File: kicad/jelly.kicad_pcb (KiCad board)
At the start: 2 copper layers, 59.9 x 32.9 mm, 29 parts, among them M1 PAGER_MOTOR, M2 PAGER_MOTOR, P1 CONN_01X01, P10 CONN_01X01, P11 CONN_01X01, P12 CONN_01X01, P13 CONN_01X01, P14 CONN_01X01, P15 CONN_01X01, P2 CONN_01X01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

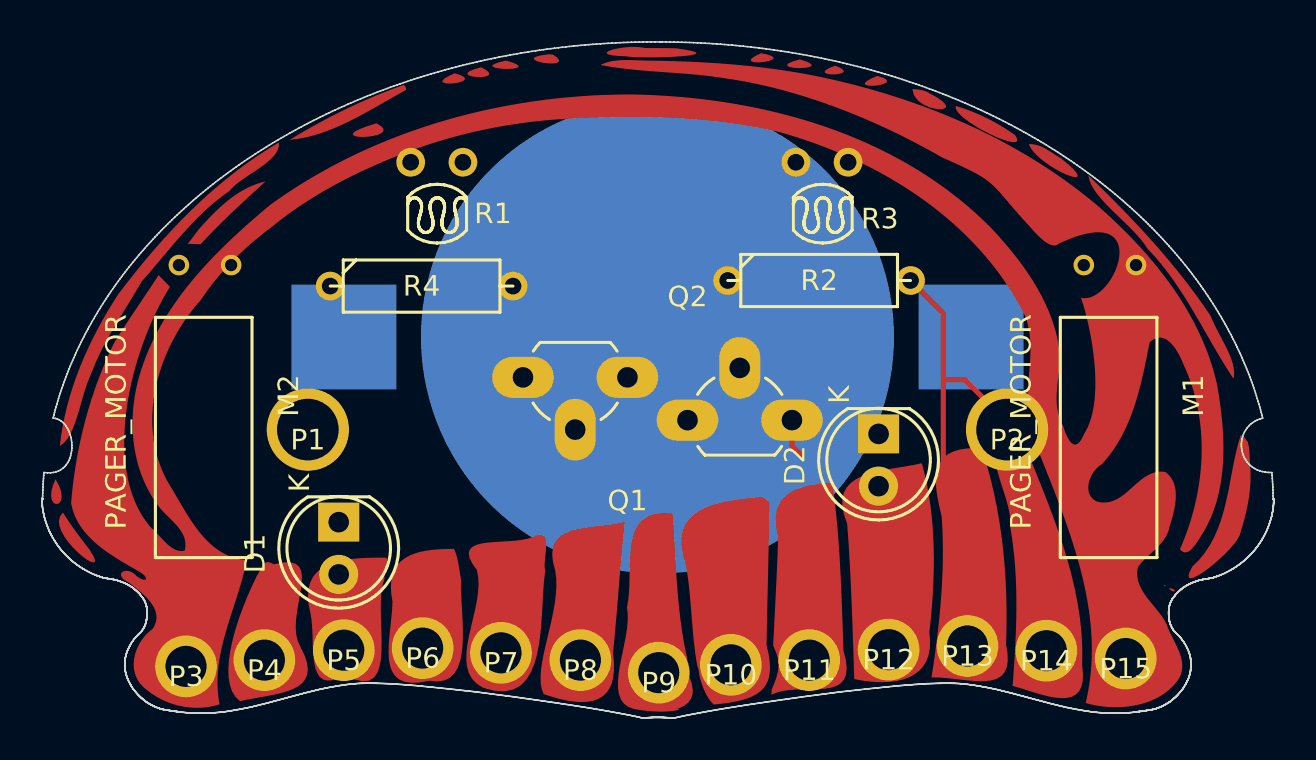
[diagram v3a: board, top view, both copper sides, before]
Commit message: Try and fit things in around CR2450
doesn't look possible
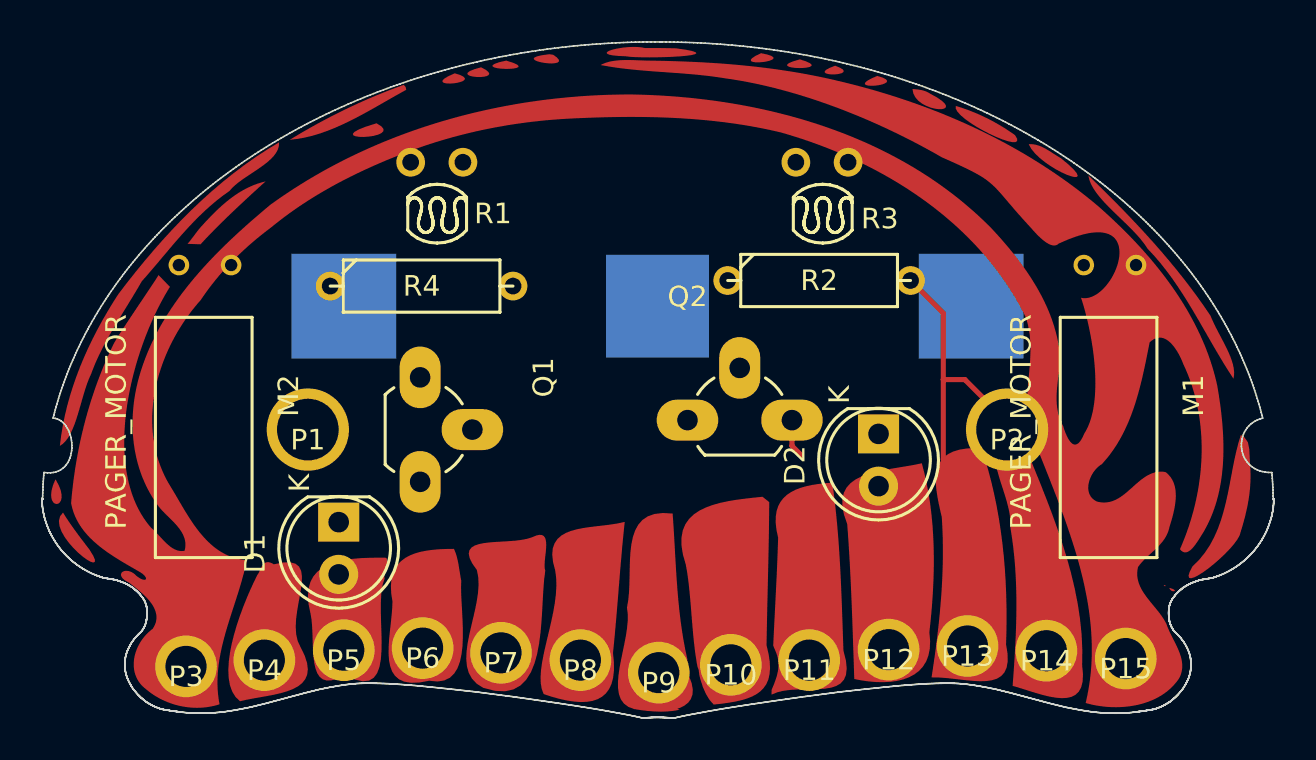
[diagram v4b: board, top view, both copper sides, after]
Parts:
- BT1: footprint custom:cr2450_holder -> cr2450_holder
- moved Q1 10.1 mm to (138.5, 80.5), turned to 270 degrees
- moved BT1 1.50 mm to (150.0, 77.0)
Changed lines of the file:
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@@
   (general
     (links 30)
-    (no_connects 26)
+    (no_connects 28)
     (area 119.662141 58.550827 180.412426 101.693013)
     (thickness 1.6)
@@
     (pad_to_mask_clearance 0)
     (aux_axis_origin 0 0)
-    (visible_elements FFFFFF7F)
+    (visible_elements FFFCFF7F)
     (pcbplotparams
       (layerselection 0x010f0_ffffffff)
@@
     (add_net Vout2)
   )
-  (module custom:cr2450_holder (layer B.Cu)
-    (at 150 78.5 180)
+  (module cr2450_holder (layer B.Cu)
+    (at 150 77 180)
     (fp_text reference BT1 (at 0 -0.5 180) (layer B.SilkS)
       (effects (font (size 1 1) (thickness 0.15)) (justify mirror))
@@
       (effects (font (size 1 1) (thickness 0.15)) (justify mirror))
     )
-    (fp_arc (start -9 8) (end -12 8) (angle -180) (layer B.SilkS) (width 0.15))
-    (fp_arc (start 9 8) (end 6 8) (angle -180) (layer B.SilkS) (width 0.15))
+    (fp_circle (center 0 0) (end 12.25 0.5) (layer B.SilkS) (width 0.15))
+    (fp_arc (start 9 5) (end 6 8) (angle -90) (layer B.SilkS) (width 0.15))
+    (fp_arc (start -9 6) (end -12 8) (angle -112.6198649) (layer B.SilkS) (width 0.15))
+    (fp_arc (start 0 12) (end 6 8) (angle -112.6198649) (layer B.SilkS) (width 0.15))
     (fp_line (start -12 8) (end -12 -7) (layer B.SilkS) (width 0.15))
     (fp_line (start -12 -7) (end -4 -14) (layer B.SilkS) (width 0.15))
@@
     (fp_line (start 4 -14) (end 12 -7) (layer B.SilkS) (width 0.15))
     (fp_line (start 12 -7) (end 12 8) (layer B.SilkS) (width 0.15))
-    (pad 1 smd rect (at -15.25 0 180) (size 5.1 5.1) (layers B.Cu B.Paste B.Mask)
+    (pad 2 smd rect (at -15.25 0 180) (size 5.1 5.1) (layers B.Cu B.Paste B.Mask)
+      (net 6 GND))
+    (pad 2 smd rect (at 15.25 0 180) (size 5.1 5.1) (layers B.Cu B.Paste B.Mask)
+      (net 6 GND))
+    (pad 1 smd rect (at 0 0 180) (size 5 5) (layers B.Cu B.Paste B.Mask)
       (net 7 "Net-(BT1-Pad1)"))
-    (pad 1 smd rect (at 15.25 0 180) (size 5.1 5.1) (layers B.Cu B.Paste B.Mask)
-      (net 7 "Net-(BT1-Pad1)"))
-    (pad 2 smd circle (at 0 0 180) (size 23 23) (layers B.Cu B.Paste B.Mask)
-      (net 6 GND))
   )
   (module KiCad/LEDs.pretty:LED-5MM (layer F.Cu)
@@
   )
   (module KiCad/TO_SOT_Packages_THT.pretty:TO-92_Rugged (layer F.Cu)
-    (at 148.54 80.46 180)
+    (at 138.46 80.46 270)
     (descr "TO-92 rugged, leads molded, wide, drill 1mm (see NXP sot054_po.pdf)")
     (tags "to-92 sc-43 sc-43a sot54 PA33 transistor")
-    (fp_text reference Q1 (at 0 -6 180) (layer F.SilkS)
-      (effects (font (size 1 1) (thickness 0.15)))
-    )
-    (fp_text value 2N7000 (at 0 3 180) (layer F.Fab)
+    (fp_text reference Q1 (at 0 -6 270) (layer F.SilkS)
+      (effects (font (size 1 1) (thickness 0.15)))
+    )
+    (fp_text value 2N7000 (at 0 3 270) (layer F.Fab)
       (effects (font (size 1 1) (thickness 0.15)))
     )
@@
     (fp_line (start -1.75 -4.3) (end 6.85 -4.3) (layer F.CrtYd) (width 0.05))
     (fp_line (start 6.85 1.95) (end 6.85 -4.3) (layer F.CrtYd) (width 0.05))
-    (pad 2 thru_hole oval (at 2.54 -2.54 270) (size 2.99974 1.99898) (drill 1) (layers *.Cu *.Mask F.SilkS)
+    (pad 2 thru_hole oval (at 2.54 -2.54) (size 2.99974 1.99898) (drill 1) (layers *.Cu *.Mask F.SilkS)
       (net 4 "Net-(Q1-Pad2)"))
-    (pad 1 thru_hole oval (at 0 0 270) (size 1.99898 2.99974) (drill 1) (layers *.Cu *.Mask F.SilkS)
+    (pad 1 thru_hole oval (at 0 0) (size 1.99898 2.99974) (drill 1) (layers *.Cu *.Mask F.SilkS)
       (net 6 GND))
-    (pad 3 thru_hole oval (at 5.08 0 270) (size 1.99898 2.99974) (drill 1) (layers *.Cu *.Mask F.SilkS)
+    (pad 3 thru_hole oval (at 5.08 0) (size 1.99898 2.99974) (drill 1) (layers *.Cu *.Mask F.SilkS)
       (net 2 Vout1))
     (model TO_SOT_Packages_THT.3dshapes/TO-92_Rugged.wrl

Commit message: Give up on CR2450
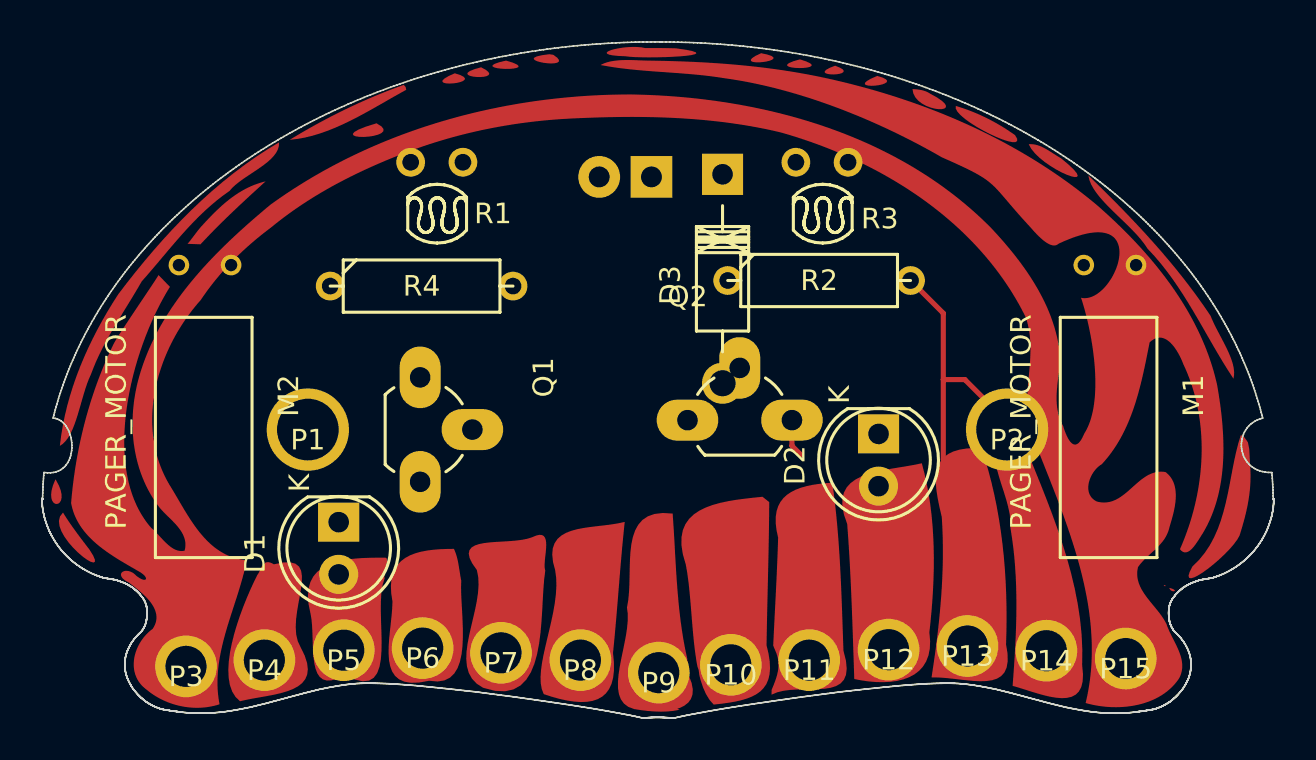
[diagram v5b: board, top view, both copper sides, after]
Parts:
- added D3: D_Small, KiCad/Diodes_ThroughHole.pretty:Diode_DO-41_SOD81_Horizontal_RM10, F.Cu at (153.2, 70.6)
- BT1: footprint cr2450_holder -> KiCad/Pin_Headers.pretty:Pin_Header_Straight_1x02
- moved BT1 6.29 mm to (149.7, 70.7), turned to 90 degrees
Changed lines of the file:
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@@
     (links 30)
     (no_connects 28)
-    (area 119.662141 58.550827 180.412426 101.693013)
+    (area 0 0 0 0)
     (thickness 1.6)
     (drawings 0)
     (tracks 12)
     (zones 0)
-    (modules 29)
-    (nets 11)
+    (modules 30)
+    (nets 12)
   )
   (page A4)
@@
   (net 9 "Net-(D1-Pad1)")
   (net 10 "Net-(D2-Pad1)")
+  (net 11 "Net-(D3-Pad1)")
   (net_class Default "This is the default net class."
     (clearance 0.2)
@@
     (add_net "Net-(D1-Pad1)")
     (add_net "Net-(D2-Pad1)")
+    (add_net "Net-(D3-Pad1)")
     (add_net "Net-(P1-Pad1)")
     (add_net "Net-(Q1-Pad2)")
@@
     (add_net Vout2)
   )
-  (module cr2450_holder (layer B.Cu)
-    (at 150 77 180)
-    (fp_text reference BT1 (at 0 -0.5 180) (layer B.SilkS)
-      (effects (font (size 1 1) (thickness 0.15)) (justify mirror))
-    )
-    (fp_text value BATTERY (at 0 0.5 180) (layer B.Fab)
-      (effects (font (size 1 1) (thickness 0.15)) (justify mirror))
-    )
-    (fp_circle (center 0 0) (end 12.25 0.5) (layer B.SilkS) (width 0.15))
-    (fp_arc (start 9 5) (end 6 8) (angle -90) (layer B.SilkS) (width 0.15))
-    (fp_arc (start -9 6) (end -12 8) (angle -112.6198649) (layer B.SilkS) (width 0.15))
-    (fp_arc (start 0 12) (end 6 8) (angle -112.6198649) (layer B.SilkS) (width 0.15))
-    (fp_line (start -12 8) (end -12 -7) (layer B.SilkS) (width 0.15))
-    (fp_line (start -12 -7) (end -4 -14) (layer B.SilkS) (width 0.15))
-    (fp_line (start -4 -14) (end 4 -14) (layer B.SilkS) (width 0.15))
-    (fp_line (start 4 -14) (end 12 -7) (layer B.SilkS) (width 0.15))
-    (fp_line (start 12 -7) (end 12 8) (layer B.SilkS) (width 0.15))
-    (pad 2 smd rect (at -15.25 0 180) (size 5.1 5.1) (layers B.Cu B.Paste B.Mask)
-      (net 6 GND))
-    (pad 2 smd rect (at 15.25 0 180) (size 5.1 5.1) (layers B.Cu B.Paste B.Mask)
-      (net 6 GND))
-    (pad 1 smd rect (at 0 0 180) (size 5 5) (layers B.Cu B.Paste B.Mask)
-      (net 7 "Net-(BT1-Pad1)"))
-  )
   (module KiCad/LEDs.pretty:LED-5MM (layer F.Cu)
     (at 134.5 87.5 270)
@@
       (xy 24.885017 10.694285)) (layer F.Cu) (width 0))
   )
+  (module KiCad/Pin_Headers.pretty:Pin_Header_Straight_1x02 (layer B.Cu)
+    (at 149.7076 70.7136 90)
+    (descr "Through hole pin header")
+    (tags "pin header")
+    (fp_text reference BT1 (at 0 5.1 90) (layer B.SilkS)
+      (effects (font (size 1 1) (thickness 0.15)) (justify mirror))
+    )
+    (fp_text value BATTERY (at 0 3.1 90) (layer B.Fab)
+      (effects (font (size 1 1) (thickness 0.15)) (justify mirror))
+    )
+    (fp_line (start 1.27 -1.27) (end 1.27 -3.81) (layer B.SilkS) (width 0.15))
+    (fp_line (start 1.55 1.55) (end 1.55 0) (layer B.SilkS) (width 0.15))
+    (fp_line (start -1.75 1.75) (end -1.75 -4.3) (layer B.CrtYd) (width 0.05))
+    (fp_line (start 1.75 1.75) (end 1.75 -4.3) (layer B.CrtYd) (width 0.05))
+    (fp_line (start -1.75 1.75) (end 1.75 1.75) (layer B.CrtYd) (width 0.05))
+    (fp_line (start -1.75 -4.3) (end 1.75 -4.3) (layer B.CrtYd) (width 0.05))
+    (fp_line (start 1.27 -1.27) (end -1.27 -1.27) (layer B.SilkS) (width 0.15))
+    (fp_line (start -1.55 0) (end -1.55 1.55) (layer B.SilkS) (width 0.15))
+    (fp_line (start -1.55 1.55) (end 1.55 1.55) (layer B.SilkS) (width 0.15))
+    (fp_line (start -1.27 -1.27) (end -1.27 -3.81) (layer B.SilkS) (width 0.15))
+    (fp_line (start -1.27 -3.81) (end 1.27 -3.81) (layer B.SilkS) (width 0.15))
+    (pad 1 thru_hole rect (at 0 0 90) (size 2.032 2.032) (drill 1.016) (layers *.Cu *.Mask B.SilkS)
+      (net 7 "Net-(BT1-Pad1)"))
+    (pad 2 thru_hole oval (at 0 -2.54 90) (size 2.032 2.032) (drill 1.016) (layers *.Cu *.Mask B.SilkS)
+      (net 6 GND))
+    (model Pin_Headers.3dshapes/Pin_Header_Straight_1x02.wrl
+      (at (xyz 0 -0.05 0))
+      (scale (xyz 1 1 1))
+      (rotate (xyz 0 0 90))
+    )
+  )
+  (module KiCad/Diodes_ThroughHole.pretty:Diode_DO-41_SOD81_Horizontal_RM10 (layer F.Cu)
+    (at 153.162 70.5866 270)
+    (descr "Diode, DO-41, SOD81, Horizontal, RM 10mm,")
+    (tags "Diode, DO-41, SOD81, Horizontal, RM 10mm, 1N4007, SB140,")
+    (fp_text reference D3 (at 5.38734 2.53746 270) (layer F.SilkS)
+      (effects (font (size 1 1) (thickness 0.15)))
+    )
+    (fp_text value D_Small (at 4.37134 -3.55854 270) (layer F.Fab)
+      (effects (font (size 1 1) (thickness 0.15)))
+    )
+    (fp_line (start 7.62 -0.00254) (end 8.636 -0.00254) (layer F.SilkS) (width 0.15))
+    (fp_line (start 2.794 -0.00254) (end 1.524 -0.00254) (layer F.SilkS) (width 0.15))
+    (fp_line (start 3.048 -1.27254) (end 3.048 1.26746) (layer F.SilkS) (width 0.15))
+    (fp_line (start 3.302 -1.27254) (end 3.302 1.26746) (layer F.SilkS) (width 0.15))
+    (fp_line (start 3.556 -1.27254) (end 3.556 1.26746) (layer F.SilkS) (width 0.15))
+    (fp_line (start 2.794 -1.27254) (end 2.794 1.26746) (layer F.SilkS) (width 0.15))
+    (fp_line (start 3.81 -1.27254) (end 2.54 1.26746) (layer F.SilkS) (width 0.15))
+    (fp_line (start 2.54 -1.27254) (end 3.81 1.26746) (layer F.SilkS) (width 0.15))
+    (fp_line (start 3.81 -1.27254) (end 3.81 1.26746) (layer F.SilkS) (width 0.15))
+    (fp_line (start 3.175 -1.27254) (end 3.175 1.26746) (layer F.SilkS) (width 0.15))
+    (fp_line (start 2.54 1.26746) (end 2.54 -1.27254) (layer F.SilkS) (width 0.15))
+    (fp_line (start 2.54 -1.27254) (end 7.62 -1.27254) (layer F.SilkS) (width 0.15))
+    (fp_line (start 7.62 -1.27254) (end 7.62 1.26746) (layer F.SilkS) (width 0.15))
+    (fp_line (start 7.62 1.26746) (end 2.54 1.26746) (layer F.SilkS) (width 0.15))
+    (pad 2 thru_hole circle (at 10.16 -0.00254 90) (size 1.99898 1.99898) (drill 1.27) (layers *.Cu *.Mask F.SilkS)
+      (net 7 "Net-(BT1-Pad1)"))
+    (pad 1 thru_hole rect (at 0 -0.00254 90) (size 1.99898 1.99898) (drill 1.00076) (layers *.Cu *.Mask F.SilkS)
+      (net 11 "Net-(D3-Pad1)"))
+  )
   (segment (start 164.9476 80.5688) (end 167.1066 82.7278) (width 0.25) (layer F.Cu) (net 1))

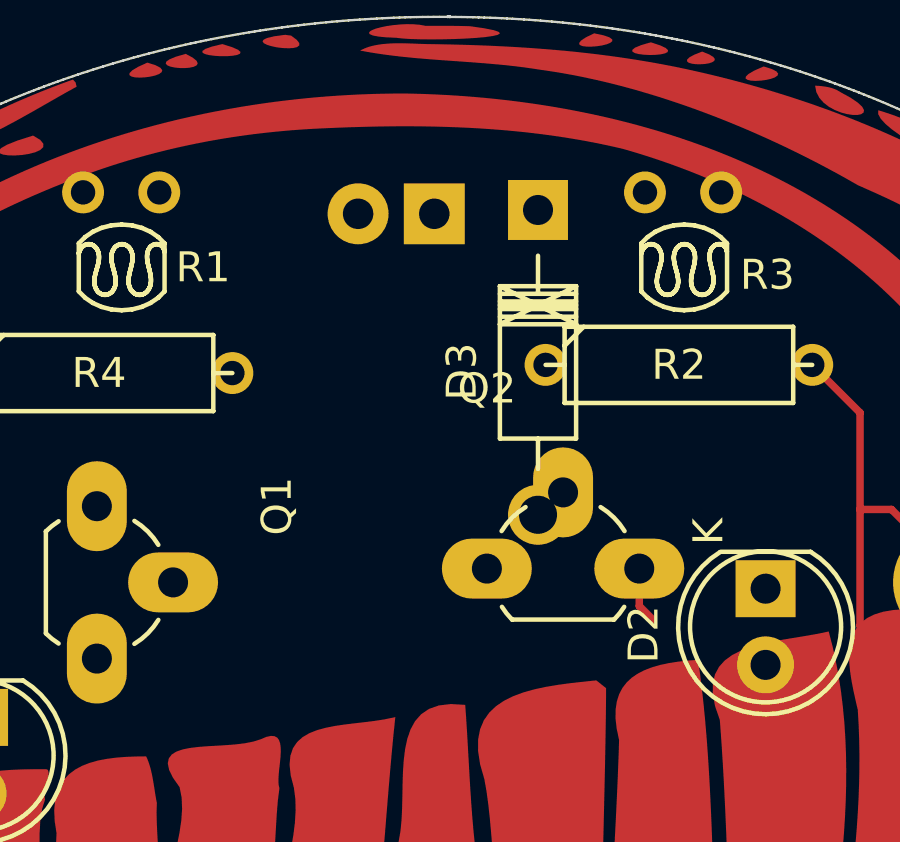
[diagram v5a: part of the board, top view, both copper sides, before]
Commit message: Turn of visibility of footprint fields in schematic
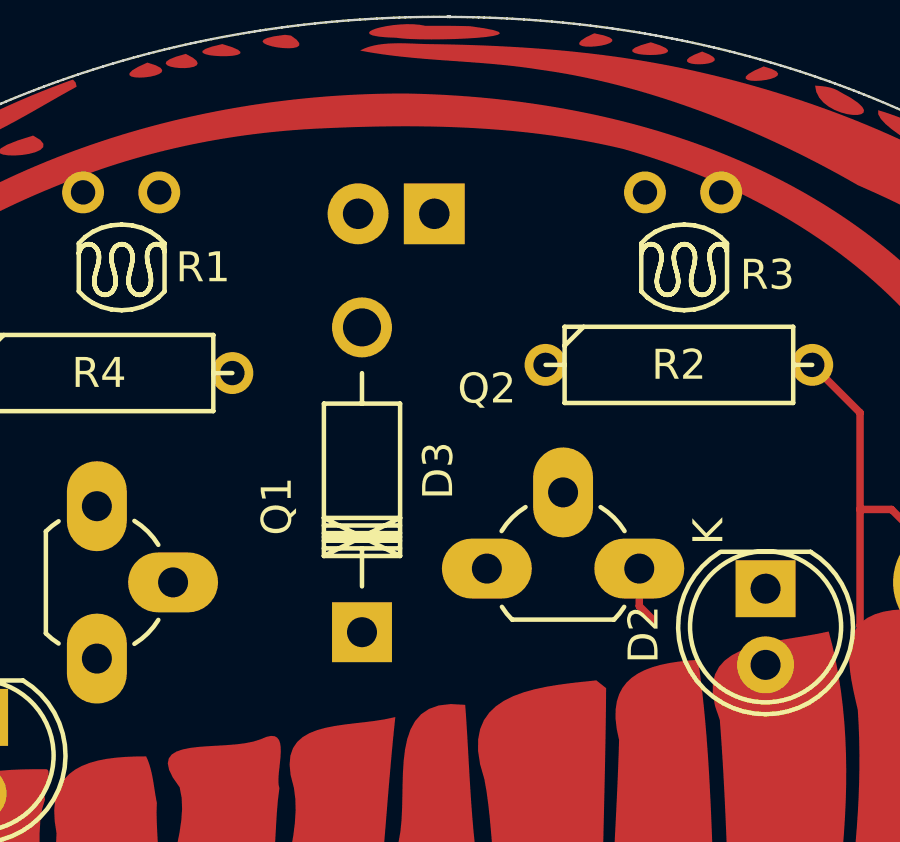
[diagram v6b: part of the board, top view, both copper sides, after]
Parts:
- moved D3 15.2 mm to (147.3, 84.7), turned to 90 degrees
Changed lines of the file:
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@@
-(kicad_pcb (version 20160815) (host pcbnew 4.1.0-alpha+201608271546+7097~46~ubuntu14.04.1-product)
+(kicad_pcb (version 20160815) (host pcbnew 4.1.0-alpha+201608281547+7098~46~ubuntu16.04.1-product)
   (general
     (links 30)
     (no_connects 28)
-    (area 0 0 0 0)
+    (area 119.662141 58.550827 180.412426 101.693013)
     (thickness 1.6)
     (drawings 0)
@@
   )
   (module KiCad/Diodes_ThroughHole.pretty:Diode_DO-41_SOD81_Horizontal_RM10 (layer F.Cu)
-    (at 153.162 70.5866 270)
+    (at 147.3 84.66 90)
     (descr "Diode, DO-41, SOD81, Horizontal, RM 10mm,")
     (tags "Diode, DO-41, SOD81, Horizontal, RM 10mm, 1N4007, SB140,")
-    (fp_text reference D3 (at 5.38734 2.53746 270) (layer F.SilkS)
+    (fp_text reference D3 (at 5.38734 2.53746 90) (layer F.SilkS)
       (effects (font (size 1 1) (thickness 0.15)))
     )
-    (fp_text value D_Small (at 4.37134 -3.55854 270) (layer F.Fab)
+    (fp_text value D_Small (at 4.37134 -3.55854 90) (layer F.Fab)
       (effects (font (size 1 1) (thickness 0.15)))
     )
@@
     (fp_line (start 7.62 -1.27254) (end 7.62 1.26746) (layer F.SilkS) (width 0.15))
     (fp_line (start 7.62 1.26746) (end 2.54 1.26746) (layer F.SilkS) (width 0.15))
-    (pad 2 thru_hole circle (at 10.16 -0.00254 90) (size 1.99898 1.99898) (drill 1.27) (layers *.Cu *.Mask F.SilkS)
+    (pad 2 thru_hole circle (at 10.16 -0.00254 270) (size 1.99898 1.99898) (drill 1.27) (layers *.Cu *.Mask F.SilkS)
       (net 7 "Net-(BT1-Pad1)"))
-    (pad 1 thru_hole rect (at 0 -0.00254 90) (size 1.99898 1.99898) (drill 1.00076) (layers *.Cu *.Mask F.SilkS)
+    (pad 1 thru_hole rect (at 0 -0.00254 270) (size 1.99898 1.99898) (drill 1.00076) (layers *.Cu *.Mask F.SilkS)
       (net 11 "Net-(D3-Pad1)"))
   )
